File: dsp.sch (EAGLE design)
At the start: 118 parts, among them IC1 OPA2134P, IC2 OPA2134P, IC3 OPA2134P, U1 STM32F405RGT6, U2 CODECODER-WM8731SEDS/V(SSOP28), U4 LM2575HVS-3.3/NOPB, X1 ABLS-8.000MHZ-B4-T

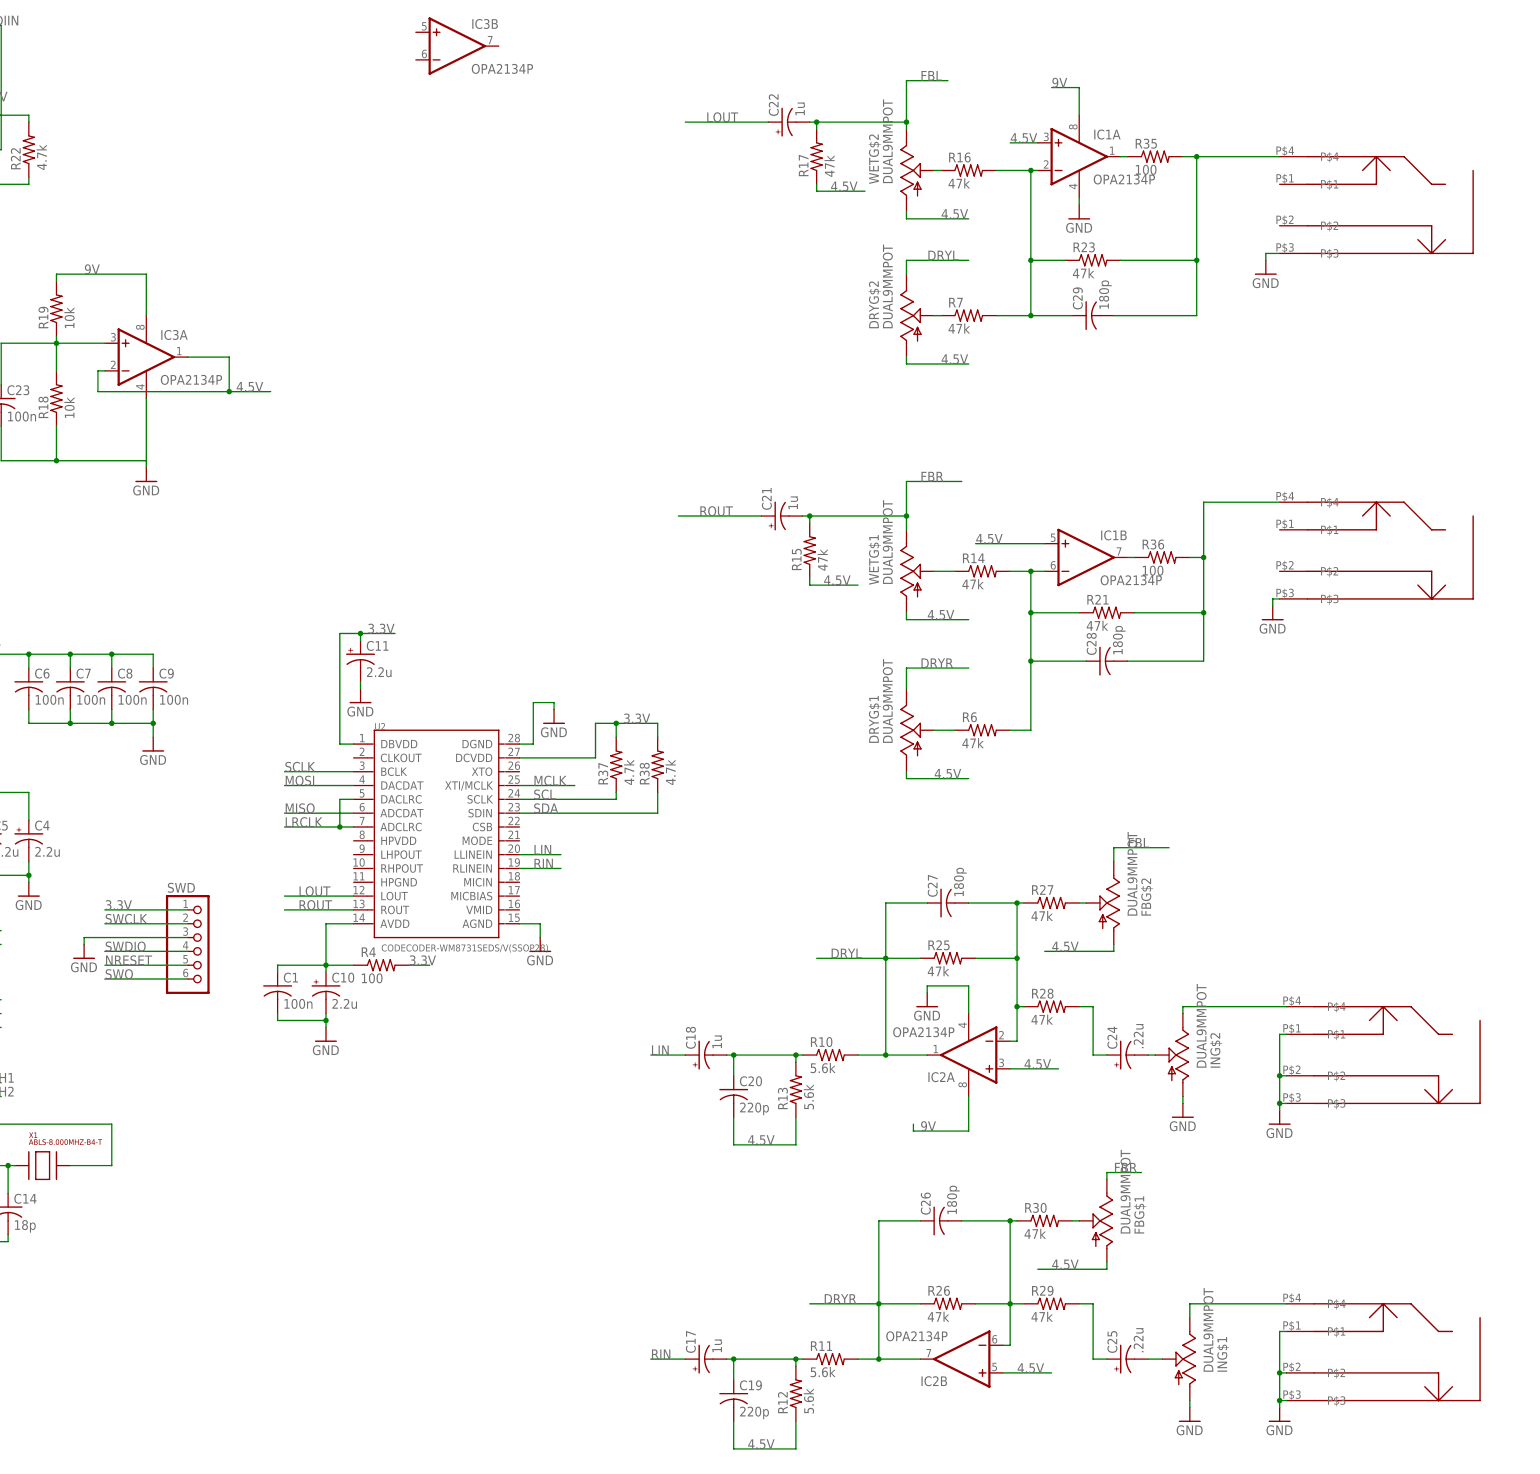
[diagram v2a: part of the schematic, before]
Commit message: mono routing, ac coupled op, jumper for feedback
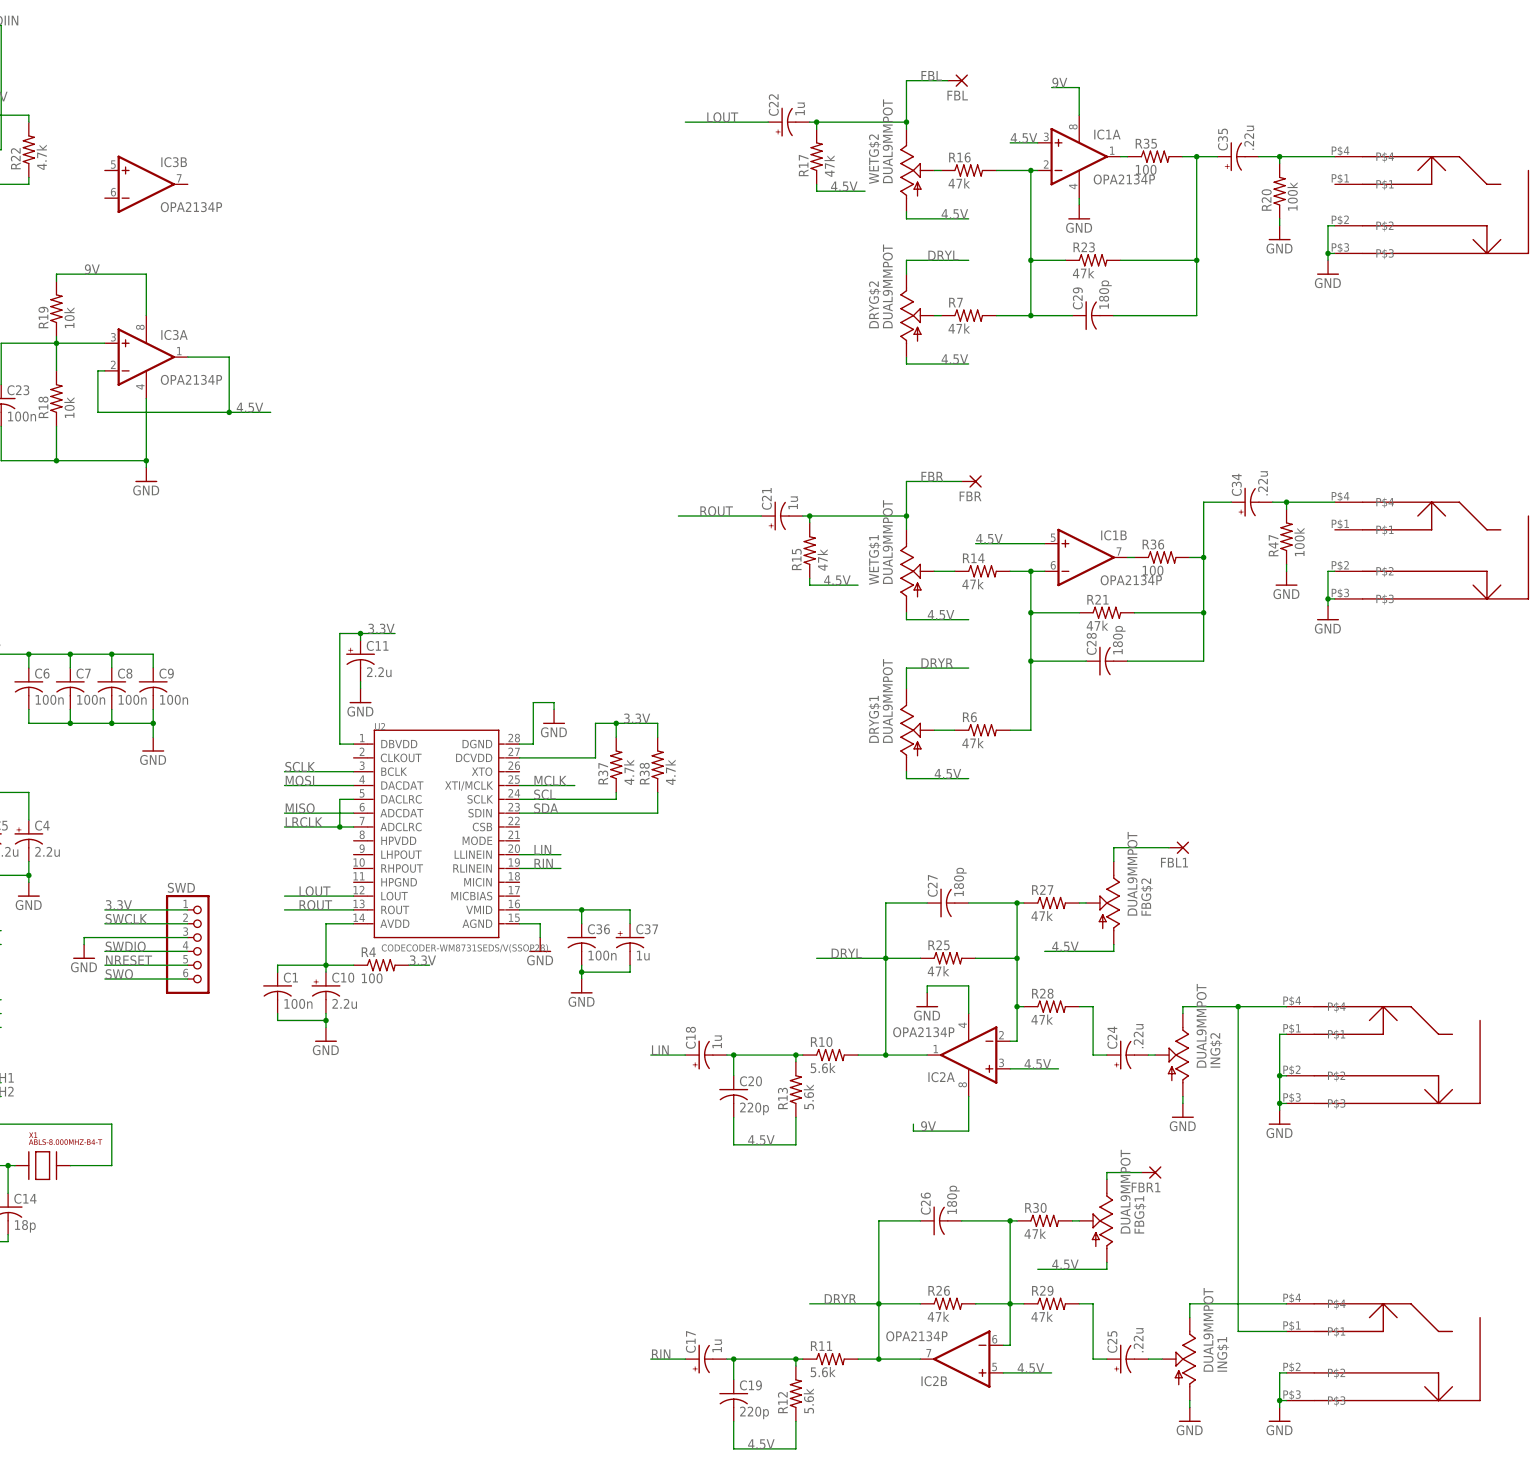
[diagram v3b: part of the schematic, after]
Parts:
- added C34, C35: .22u, dan:CPOL-USE2.5-7
- added C36: 100n, dan:C-US050-025X075
- added C37: 1u, dan:CPOL-USE2-4
- added FBL, FBL1, FBR, FBR1: (no value), synthdiy:2,0/0,9-S
- added R20, R47: 100k, dan:R-US_0309/V
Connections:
- removed net N$25: ING$2.E, INL.P$4
- new net N$53: C35.-, OUTL.P$4, R20.2
- new net N$54: C34.-, OUTR.P$4, R47.2
- new net N$55: FBG$2.E, FBL1.P
- new net N$56: FBG$1.E, FBR1.P
- new net N$57: C36.1, C37.+, U2.VMID
- new net N$58: ING$2.E, INL.P$4, INR.P$1
- net FBL: now also FBL.P; no longer FBG$2.E
- net FBR: now also FBR.P; no longer FBG$1.E
- net GND: now also C36.2, C37.-, OUTL.P$2, OUTR.P$2, R20.1, R47.1; no longer INR.P$1
- net N$23: now also C34.+; no longer OUTR.P$4
- net N$24: now also C35.+; no longer OUTL.P$4
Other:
- moved on the sheet: IC3B

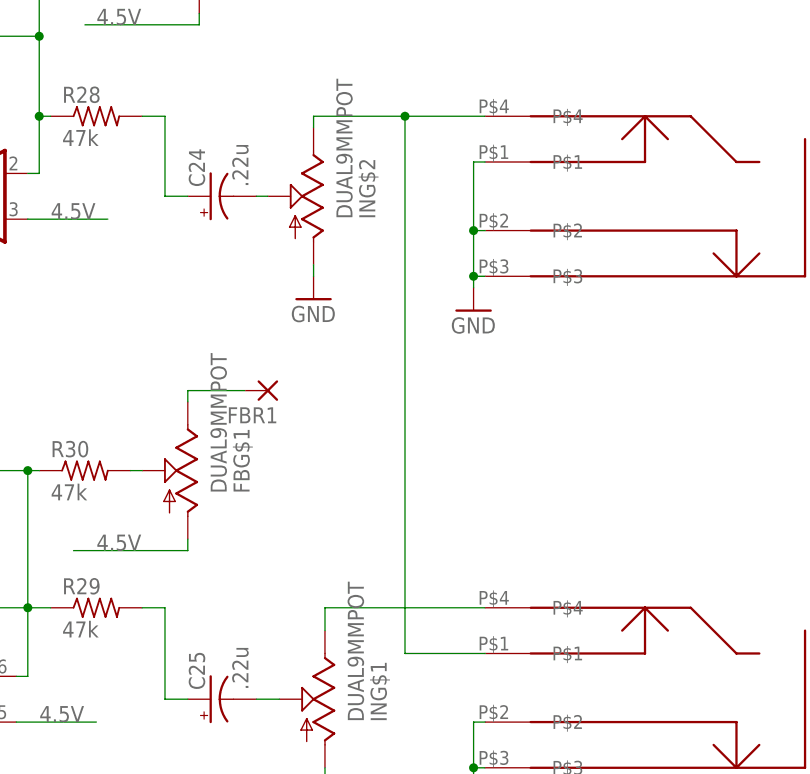
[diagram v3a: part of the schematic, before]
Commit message: routing for mono on both inputs
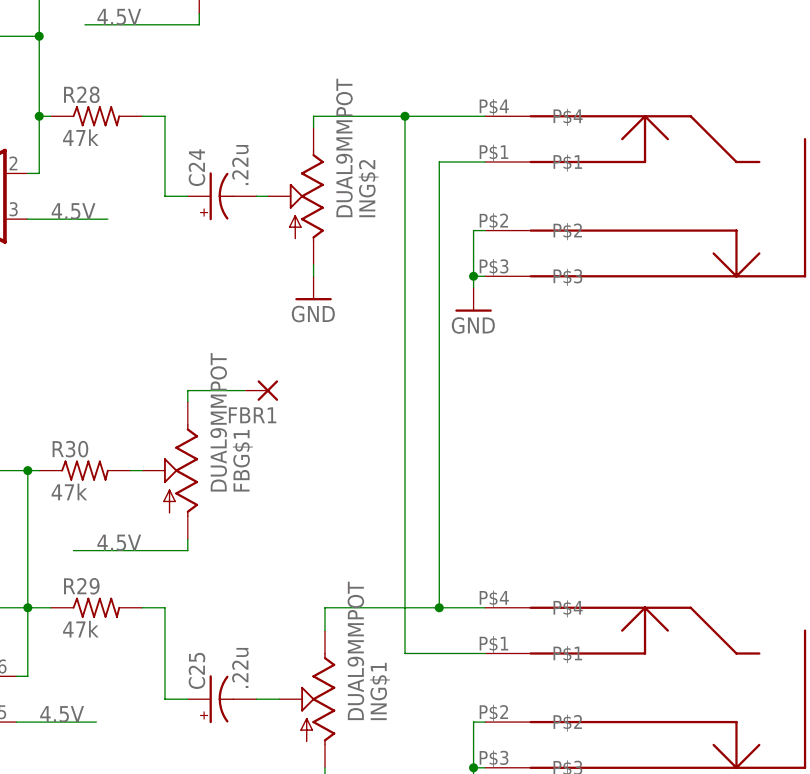
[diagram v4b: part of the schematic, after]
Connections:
- net GND: no longer INL.P$1
- net N$29: now also INL.P$1
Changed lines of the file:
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@@
 <pinref part="GND23" gate="1" pin="GND"/>
 <wire x1="328.93" y1="36.83" x2="328.93" y2="35.56" width="0.1524" layer="91"/>
-<pinref part="INL" gate="G$1" pin="P$1"/>
-<wire x1="330.2" y1="49.53" x2="328.93" y2="49.53" width="0.1524" layer="91"/>
-<wire x1="328.93" y1="49.53" x2="328.93" y2="41.91" width="0.1524" layer="91"/>
 <pinref part="INL" gate="G$1" pin="P$2"/>
 <wire x1="328.93" y1="41.91" x2="328.93" y2="36.83" width="0.1524" layer="91"/>
 <wire x1="330.2" y1="41.91" x2="328.93" y2="41.91" width="0.1524" layer="91"/>
 <junction x="328.93" y="36.83"/>
-<junction x="328.93" y="41.91"/>
 </segment>
 <segment>
@@
 <segment>
 <pinref part="INR" gate="G$1" pin="P$4"/>
-<wire x1="330.2" y1="0" x2="312.42" y2="0" width="0.1524" layer="91"/>
+<wire x1="330.2" y1="0" x2="325.12" y2="0" width="0.1524" layer="91"/>
 <pinref part="IN" gate="G$1" pin="E"/>
+<wire x1="325.12" y1="0" x2="312.42" y2="0" width="0.1524" layer="91"/>
 <wire x1="312.42" y1="-2.54" x2="312.42" y2="0" width="0.1524" layer="91"/>
-</segment>
-</net>
+<pinref part="INL" gate="G$1" pin="P$1"/>
+<wire x1="330.2" y1="49.53" x2="325.12" y2="49.53" width="0.1524" layer="91"/>
+<wire x1="325.12" y1="49.53" x2="325.12" y2="0" width="0.1524" layer="91"/>
+<junction x="325.12" y="0"/>
+</segment>
+</net>

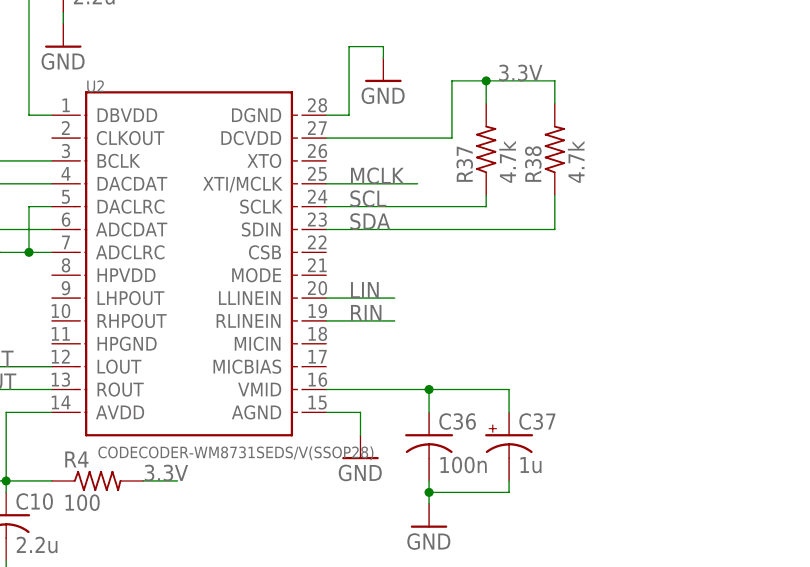
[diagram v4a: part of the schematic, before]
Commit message: connected mode and csb on wm8731
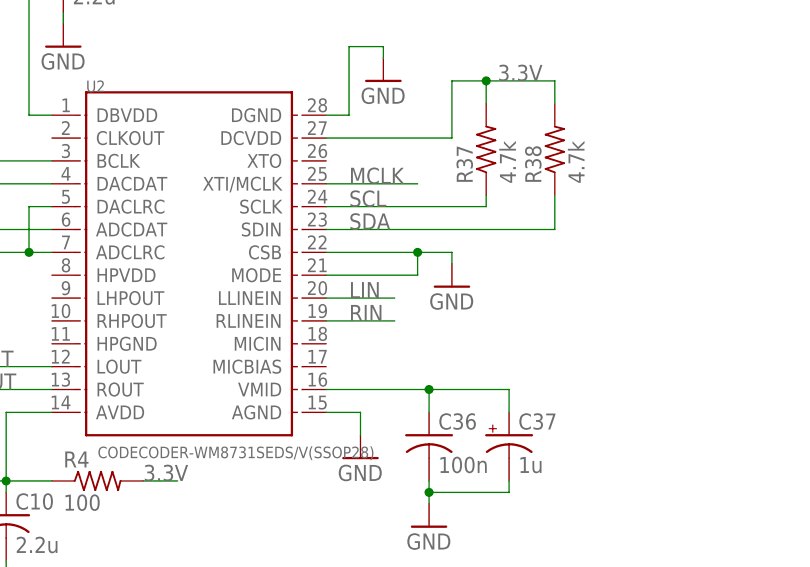
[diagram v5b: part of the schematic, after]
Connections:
- net GND: now also U2.CSB, U2.MODE
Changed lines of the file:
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@@
 <part name="GND29" library="dan" deviceset="GND" device=""/>
 <part name="C37" library="dan" deviceset="CPOL-US" device="E2-4" value="1u"/>
+<part name="GND30" library="dan" deviceset="GND" device=""/>
 </parts>
 <sheets>
@@
 <instance part="GND29" gate="1" x="200.66" y="57.15"/>
 <instance part="C37" gate="G$1" x="209.55" y="67.31"/>
+<instance part="GND30" gate="1" x="203.2" y="83.82"/>
 </instances>
 <busses>
@@
 <junction x="200.66" y="60.96"/>
 </segment>
+<segment>
+<pinref part="GND30" gate="1" pin="GND"/>
+<wire x1="203.2" y1="86.36" x2="203.2" y2="87.63" width="0.1524" layer="91"/>
+<pinref part="U2" gate="G$1" pin="MODE"/>
+<wire x1="189.23" y1="85.09" x2="199.39" y2="85.09" width="0.1524" layer="91"/>
+<wire x1="199.39" y1="85.09" x2="199.39" y2="87.63" width="0.1524" layer="91"/>
+<pinref part="U2" gate="G$1" pin="CSB"/>
+<wire x1="199.39" y1="87.63" x2="189.23" y2="87.63" width="0.1524" layer="91"/>
+<wire x1="203.2" y1="87.63" x2="199.39" y2="87.63" width="0.1524" layer="91"/>
+<junction x="199.39" y="87.63"/>
+</segment>
 </net>
